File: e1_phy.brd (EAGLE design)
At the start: 100 x 75 mm, 136 parts, among them IC2 LD117AS33TR, IC3 LD117AS33TR, IC4 MCP4725, U1 XRT82D20, U2 GPS_GNS_2201, U3 VCTCXO-CONNORWINFIELD, U4 VCXO_TAITIEN_VT, X2 SMA-142-0701-801/806, X3 JACK2.5_SJ-2523, X4 0446200002

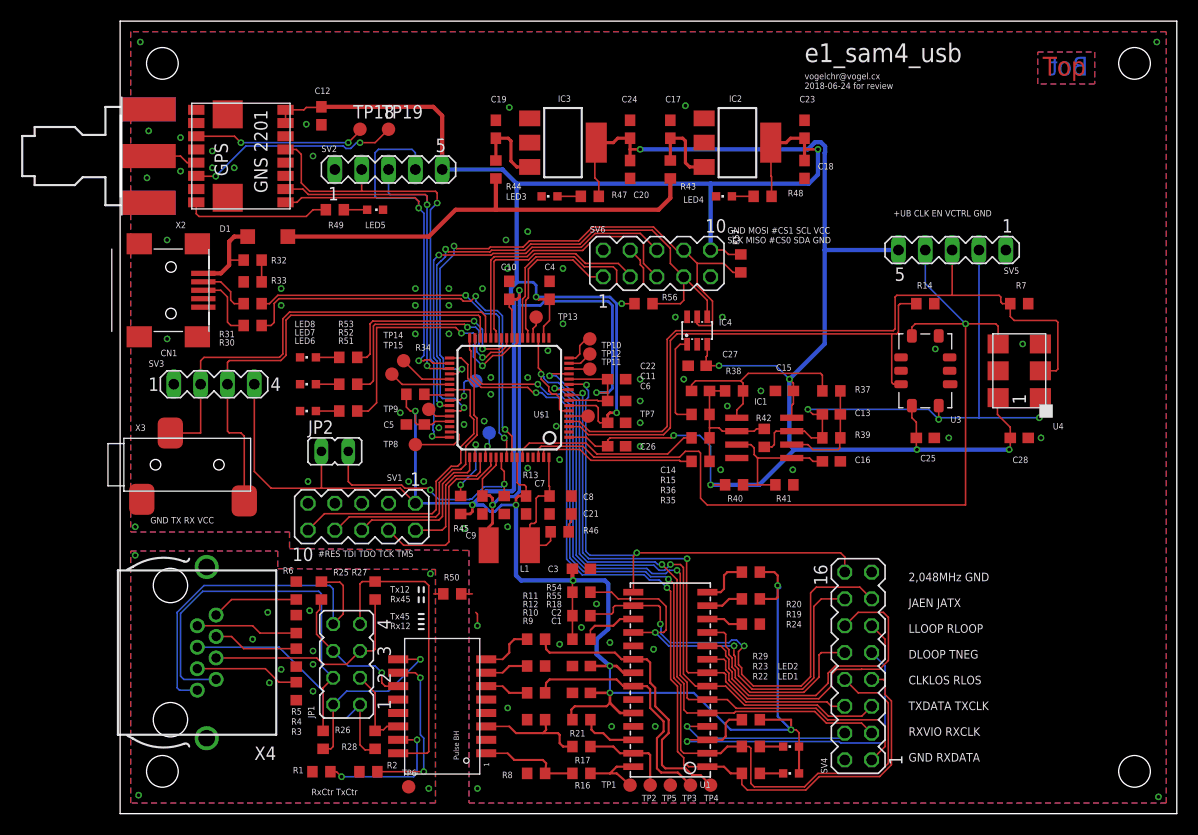
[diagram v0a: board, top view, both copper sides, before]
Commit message: Changed LIU to IDT82V2081.
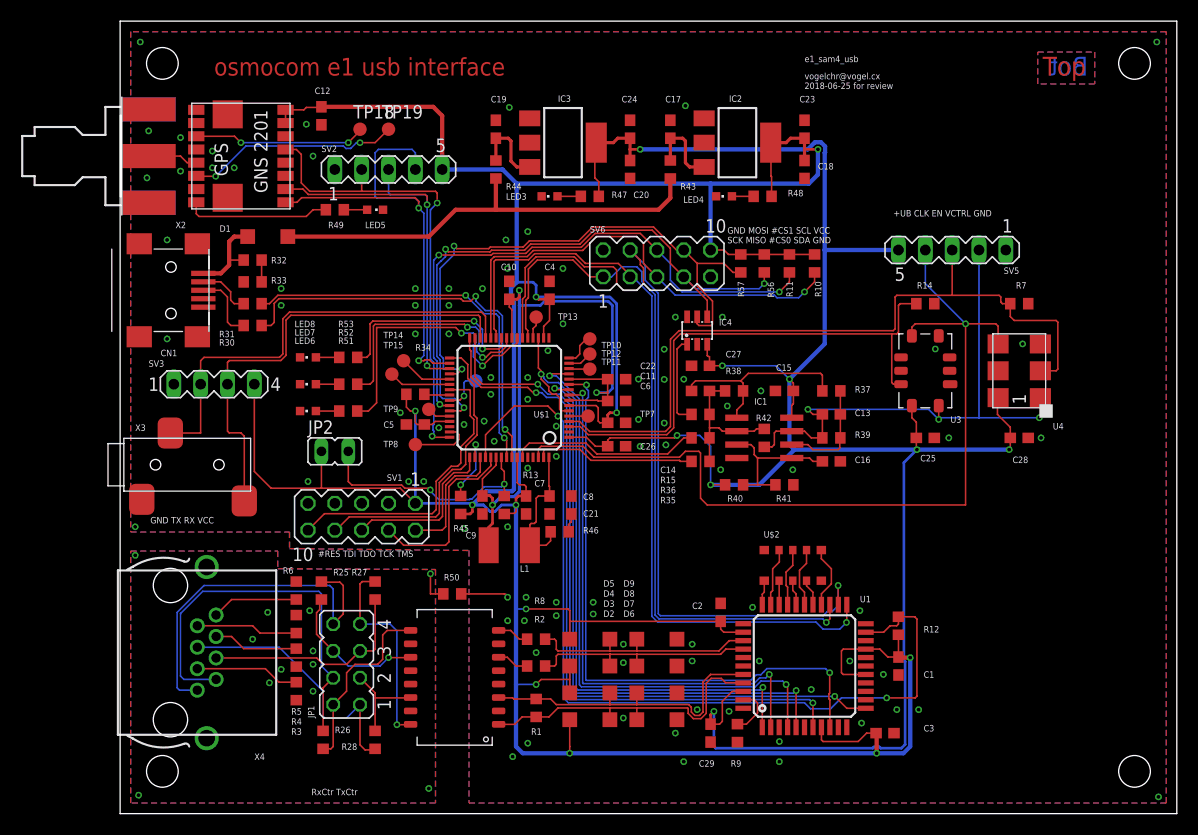
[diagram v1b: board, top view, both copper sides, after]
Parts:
- removed LED1, LED2: (no value), led:CHIPLED_0603
- removed R16, R17: 0R, rcl:R0603
- removed R18, R19, R20, R24: DNP, rcl:R0603
- removed R21, R22, R23, R29, R54, R55: 1k, rcl:R0603
- removed SV4: (no value), con-lstb:MA08-2
- removed TP1, TP17, TP2, TP3, TP4, TP5, TP6: TPB1,27, testpad:B1,27
- added C29: 100n, rcl:C0603
- added D2, D3, D4, D5, D6, D7, D8, D9: MBR0520LT, diode:SOD123
- added U$2: MNR 8x10k, laforge:MNR35
- C3: value 10u -> 100n
- R10, R11: value 9R1 -> 10k
- R12: value DNP -> 10k
- R8: value 60R -> DNP
- R9: value 60R -> 3k 1%
- TR1: value PE-65861 -> PULSE_T1094NL; device cvogel:PULSE_BH_XFORMER -> laforge:PULSE_BH
- U1: value XRT82D20 -> IDT82V2081; device cvogel:SOJ28/3 -> idt82v2081:TQFP44
- moved R10 48.4 mm to (65.7, 52.1), turned to 90 degrees
- moved R11 42.9 mm to (63.3, 52.1), turned to 90 degrees
- moved R12 34.5 mm to (73.7, 17.8), turned to 90 degrees
- moved C3 32.7 mm to (72.4, 7.62)
- moved C1 30.1 mm to (73.7, 14.0), turned to 270 degrees
- moved R1 21.2 mm to (39.4, 10.0), turned to 90 degrees
- moved R9 19.1 mm to (58.4, 7.62), turned to 270 degrees
- moved R2 18.8 mm to (39.4, 14.0), turned to 180 degrees
- moved C2 14.1 mm to (56.8, 19.1), turned to 90 degrees
- moved U1 12.8 mm to (64.8, 14.0)
- moved R8 12.7 mm to (39.4, 16.5)
- moved R56 12.0 mm to (61.0, 52.1), turned to 90 degrees
- moved TR1 2.77 mm to (31.6, 12.7), turned to 180 degrees
- moved C27 0.32 mm to (54.9, 42.4)
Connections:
- removed net #ATM: R24.1, U1.12
- removed net #CLKLOS: R23.1, SV4.8, U$1.31, U1.2
- removed net #DLOOP: SV4.10, U1.11
- removed net #LLOOP: SV4.12, U1.9
- removed net #RLOOP: SV4.11, U1.10
- removed net #RLOS: R22.1, SV4.7, U$1.32, U1.1
- removed net DIGI: R18.1, U1.17
- removed net JAEN: R54.2, SV4.14, U1.18
- removed net JATX: R55.2, SV4.13, U1.16
- removed net MUTERX: R21.1, U1.26
- removed net N$1: LED1.C, R22.2
- removed net N$2: LED2.C, R23.2
- removed net RAOS: R19.2, U1.13
- removed net RRING_LIU: R17.2, TP2.TP, U1.27
- removed net RTIP_LIU: R16.2, TP1.TP, U1.28
- removed net RX_PRI_CTR: R1.2, TR1.15
- removed net RX_VIOLATION: SV4.4, U1.4
- removed net TAOS: R20.2, U1.14
- removed net TNEG_CODE: R29.1, SV4.9, U1.3
- removed net TRING_XFMR: R11.1, TR1.8
- removed net TTIP_XFMR: R10.1, TR1.6
- removed net TX_PRI_CTR: R12.1, TR1.7
- removed net TX_SEC_CTR: R2.2, TR1.10
- new net #RST_LIU: U$1.31, U1.12
- new net #SPI_CS2: R11.1, SV6.6, U$1.42
- new net AD0: U$2.6, U1.26
- new net AD1: U$2.4, U1.27
- new net AD2: U$2.7, U1.28
- new net AD3: U$2.3, U1.29
- new net AD4: U$2.8, U1.30
- new net AD5: U$2.2, U1.31
- new net AD6: U$2.9, U1.32
- new net AD7: U$2.1, U1.33
- new net LOS_LIU: U$1.32, U1.7
- new net N$25: R8.2, TR1.8
- new net N$31: R9.1, U1.43
- net #SPI_CS0: now also R10.1
- net #SPI_CS1: now also R12.2, U$1.52, U1.21; no longer SV6.6, U$1.42
- net +UB: now also C29.1, U1.42
- net CLK2048: now also U1.9; no longer SV4.16, U1.15
- net GND: now also C29.2, D6.A, D7.A, D8.A, D9.A, U$2.10, U$2.5, U1.10, U1.11, U1.13, U1.14, U1.15, U1.17, U1.18, U1.22, U1.3, U1.38, U1.39, U1.44; no longer R12.2, R24.2, R8.2, SV4.15, SV4.2, TP5.TP, TR1.2, U1.19, U1.23, U1.25
- net GNDIO: no longer R1.1, R2.1, TP6.TP
- net N$5: now also R2.2, TR1.6; no longer TP17.TP, U$1.52
- net RRING: now also D3.A, D7.C, R1.2, U1.40; no longer R17.1, R9.1
- net RTIP: now also D2.A, D6.C, R1.1, U1.41; no longer R16.1, R8.1
- net RX_CLK: now also U1.4; no longer SV4.3, U1.5
- net RX_DATA: now also U1.5; no longer SV4.1, U1.6
- net SPI_MISO: now also U1.23
- net SPI_MOSI: now also U1.24
- net SPI_SCK: now also U1.25
- net TRING: now also D5.A, D9.C, R8.1, U1.36; no longer R11.2, TP4.TP, U1.20
- net TTIP: now also D4.A, D8.C, R2.1, U1.37; no longer R10.2, TP3.TP, U1.22
- net TX_CLK: now also U1.1; no longer SV4.5, U1.7
- net TX_DATA: now also U1.2; no longer SV4.6, U1.8
- net VCC: now also D2.C, D3.C, D4.C, D5.C, R10.2, R11.2, R12.1, U1.16, U1.19, U1.35, U1.8; no longer LED1.A, LED2.A, R18.2, R19.1, R20.1, R21.2, R29.2, R54.1, R55.1, U1.21, U1.24
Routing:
- net #CLKLOS: track 90.4 -> 0.00 mm, vias 2 -> 0
- net #RLOS: track 88.3 -> 0.00 mm, vias 2 -> 0
- net #RST_LIU: track 0.00 -> 69.8 mm, vias 0 -> 2
- net LOS_LIU: track 0.00 -> 67.3 mm, vias 0 -> 2
- net SPI_MOSI: track 24.4 -> 82.2 mm, vias 0 -> 1
- net +UB: track 140.7 -> 197.5 mm, vias 7 -> 8
- net SPI_SCK: track 14.8 -> 70.4 mm, vias 0 -> 1
- net #SPI_CS2: track 0.00 -> 54.1 mm, vias 0 -> 3
- net SPI_MISO: track 21.5 -> 75.5 mm, vias 0 -> 1
- net #SPI_CS1: track 37.7 -> 85.0 mm
- net JATX: track 43.2 -> 0.00 mm, vias 2 -> 0
- net JAEN: track 42.2 -> 0.00 mm, vias 2 -> 0
- net VCC: track 309.2 -> 347.7 mm, vias 12 -> 11
- net TNEG_CODE: track 34.5 -> 0.00 mm, vias 1 -> 0
- net #LLOOP: track 30.7 -> 0.00 mm
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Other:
- board text added: "osmocom e1 usb interface"
- board text added: "vogelchr@vogel.cx 2018-06-25 for review"
- board text removed: "2,048MHz GND JAEN JATX LLOOP RLOOP DLOOP TNEG CLKLOS RLOS TXDATA TXCLK RXVIO RXCLK GND RXDATA"
- board text removed: "Tx12 Rx45"
- board text removed: "Tx45 Rx12"
- board text removed: "vogelchr@vogel.cx 2018-06-24 for review"

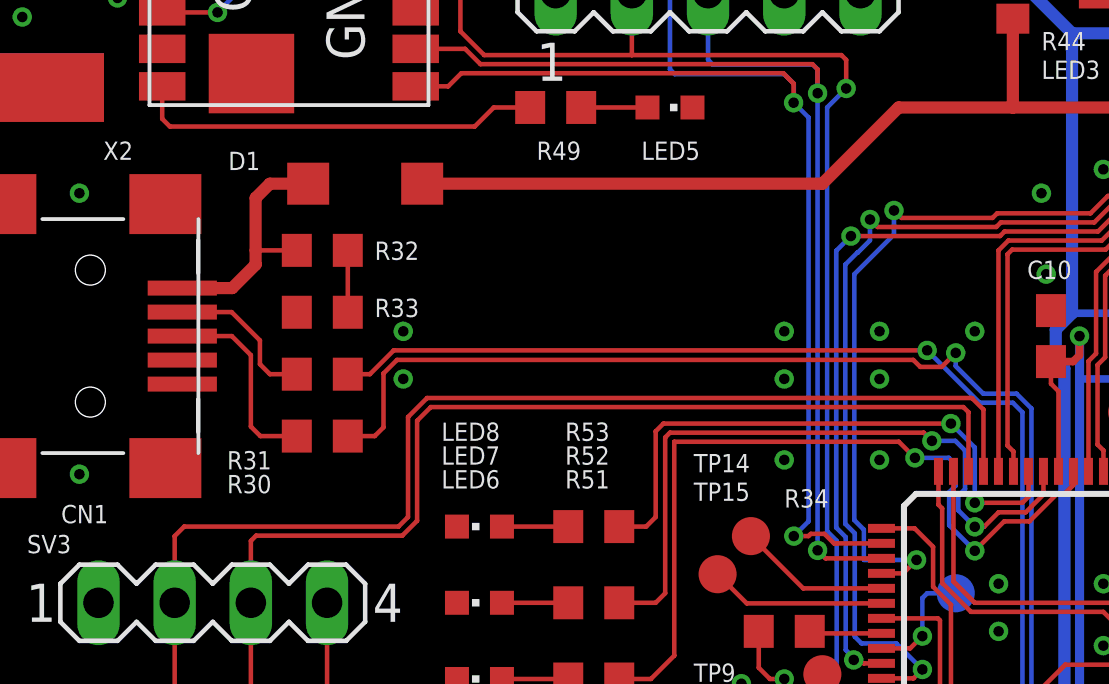
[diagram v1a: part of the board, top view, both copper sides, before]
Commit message: Implement review: ESD protection on USB.
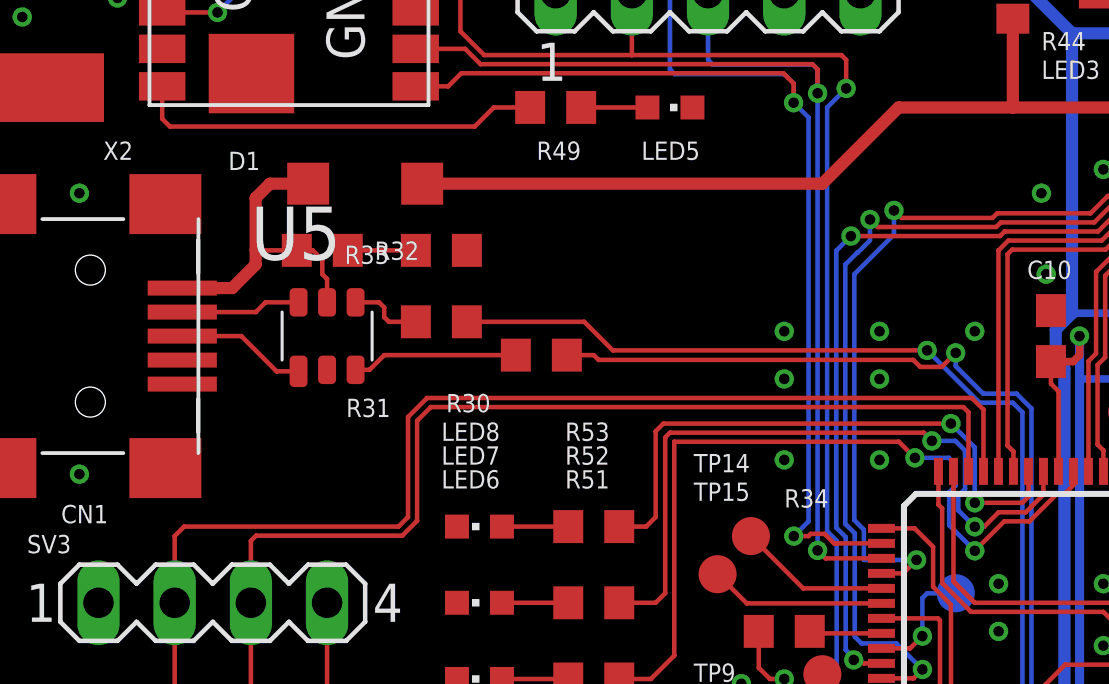
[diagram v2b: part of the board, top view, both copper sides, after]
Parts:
- added U5: IP4234CZ6, laforge:TSOP-6
- moved R30 7.79 mm to (19.8, 48.9)
- moved R33 4.47 mm to (16.5, 52.4), turned to 180 degrees
- moved R31 4.34 mm to (16.5, 50.0)
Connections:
- net USB_VBUS_CON renamed USB_VBUS
- removed net N$12: CN1.VBUS, D1.A, R32.2
- new net N$1: CN1.D+, U5.1
- new net N$2: CN1.D-, U5.6
- new net VBUS_CONN: CN1.VBUS, D1.A, R32.2, U5.5
- net GND: now also U5.2
- net USB_DDM_CON: now also U5.4; no longer CN1.D-
- net USB_DDP_CON: now also U5.3; no longer CN1.D+
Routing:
- net VBUS_CONN: track 0.00 -> 11.3 mm
- net USB_DDP: track 40.0 -> 30.7 mm
- net N$12: track 8.85 -> 0.00 mm
- net N$1: track 0.00 -> 4.36 mm
- net N$2: track 0.00 -> 4.01 mm
- net USB_DDM: track 37.2 -> 33.3 mm
- net USB_DDM_CON: track 5.14 -> 2.46 mm
- net USB_DDP_CON: track 6.59 -> 5.55 mm
- net GND: vias 98 -> 96
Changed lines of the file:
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@@
 <attribute name="VALUE" x="-2.54" y="52.84" size="1.27" layer="27" rot="R270"/>
 </element>
-<element name="R30" library="rcl" package="R0603" value="33R" x="12.54125" y="46.19625" smashed="yes" rot="R180">
-<attribute name="NAME" x="9.36625" y="44.29125" size="0.6096" layer="25" font="vector"/>
-<attribute name="VALUE" x="13.17625" y="48.10125" size="1.27" layer="27" rot="R180"/>
-</element>
-<element name="R31" library="rcl" package="R0603" value="33R" x="12.54125" y="48.26" smashed="yes" rot="R180">
-<attribute name="NAME" x="9.36625" y="45.085" size="0.6096" layer="25" font="vector"/>
-<attribute name="VALUE" x="13.17625" y="50.165" size="1.27" layer="27" rot="R180"/>
+<element name="R30" library="rcl" package="R0603" value="33R" x="19.84375" y="48.895" smashed="yes" rot="R180">
+<attribute name="NAME" x="16.66875" y="46.99" size="0.6096" layer="25" font="vector"/>
+<attribute name="VALUE" x="20.47875" y="50.8" size="1.27" layer="27" rot="R180"/>
+</element>
+<element name="R31" library="rcl" package="R0603" value="33R" x="16.51" y="50.00625" smashed="yes" rot="R180">
+<attribute name="NAME" x="13.335" y="46.83125" size="0.6096" layer="25" font="vector"/>
+<attribute name="VALUE" x="17.145" y="51.91125" size="1.27" layer="27" rot="R180"/>
 </element>
 <element name="R32" library="rcl" package="R0603" value="27k" x="12.54125" y="52.3875" smashed="yes" rot="R180">
@@
 <attribute name="VALUE" x="13.17625" y="54.2925" size="1.27" layer="27" rot="R180"/>
 </element>
-<element name="R33" library="rcl" package="R0603" value="47k" x="12.54125" y="50.32375" smashed="yes">
-<attribute name="NAME" x="14.2875" y="50.165" size="0.6096" layer="25" font="vector"/>
-<attribute name="VALUE" x="11.90625" y="48.41875" size="1.27" layer="27"/>
+<element name="R33" library="rcl" package="R0603" value="47k" x="16.51" y="52.3875" smashed="yes" rot="R180">
+<attribute name="NAME" x="14.76375" y="52.54625" size="0.6096" layer="25" font="vector" rot="R180"/>
+<attribute name="VALUE" x="17.145" y="54.2925" size="1.27" layer="27" rot="R180"/>
 </element>
 <element name="R34" library="rcl" package="R0603" value="DNP" x="27.94" y="39.6875" smashed="yes">
@@
 <attribute name="NAME" x="47.63625" y="21.47875" size="0.6096" layer="25" font="vector"/>
 <attribute name="VALUE" x="49.7" y="14.21" size="1.27" layer="27"/>
+</element>
+<element name="U5" library="laforge" package="TSOP-6" value="IP4234CZ6" x="12.7" y="49.53">
+<attribute name="OC_DIGIKEY" value="568-5869-1-ND" x="12.7" y="49.53" size="1.778" layer="27" display="off"/>
 </element>
 </elements>
@@
 <via x="27.94" y="49.68875" extent="1-16" drill="0.35"/>
 <via x="27.94" y="48.10125" extent="1-16" drill="0.35"/>
-<via x="15.24" y="48.10125" extent="1-16" drill="0.35"/>
-<via x="15.24" y="49.68875" extent="1-16" drill="0.35"/>
 <via x="31.115" y="45.4025" extent="1-16" drill="0.35"/>
 <via x="27.94" y="45.4025" extent="1-16" drill="0.35"/>
@@
 <wire x1="32.2825" y1="20.79625" x2="36.35375" y2="20.79625" width="0.1524" layer="1"/>
 <wire x1="36.35375" y1="20.79625" x2="36.67125" y2="20.47875" width="0.1524" layer="1" curve="-90"/>
+<contactref element="U5" pad="2"/>
 </signal>
 <signal name="LINE_PIN1">
@@
 <wire x1="68.77" y1="9.97" x2="67.6426" y2="11.0974" width="0.1524" layer="1"/>
 </signal>
-<signal name="USB_VBUS_CON">
+<signal name="USB_VBUS">
 <contactref element="R44" pad="2"/>
 <contactref element="R43" pad="2"/>
@@
 </signal>
 <signal name="USB_DDM_CON">
-<contactref element="CN1" pad="D-"/>
 <contactref element="R31" pad="2"/>
-<wire x1="7.874" y1="50.33" x2="9.51875" y2="50.33" width="0.1524" layer="1"/>
-<wire x1="11.69125" y1="48.26" x2="10.795" y2="48.26" width="0.1524" layer="1"/>
-<wire x1="10.4624" y1="48.5926" x2="10.795" y2="48.26" width="0.1524" layer="1"/>
-<wire x1="9.51875" y1="50.33" x2="10.4624" y2="49.38635" width="0.1524" layer="1"/>
-<wire x1="10.4624" y1="49.38635" x2="10.4624" y2="48.5926" width="0.1524" layer="1"/>
+<contactref element="U5" pad="4"/>
+<wire x1="13.65" y1="50.655" x2="14.4325" y2="50.655" width="0.1524" layer="1"/>
+<wire x1="14.4325" y1="50.655" x2="14.605" y2="50.4825" width="0.1524" layer="1"/>
+<wire x1="14.605" y1="50.4825" x2="14.605" y2="50.165" width="0.1524" layer="1"/>
+<wire x1="14.605" y1="50.165" x2="14.76375" y2="50.00625" width="0.1524" layer="1"/>
+<wire x1="14.76375" y1="50.00625" x2="15.66" y2="50.00625" width="0.1524" layer="1"/>
 </signal>
 <signal name="USB_DDP_CON">
-<contactref element="CN1" pad="D+"/>
 <contactref element="R30" pad="2"/>
-<wire x1="7.874" y1="49.53" x2="9.525" y2="49.53" width="0.1524" layer="1"/>
-<wire x1="9.525" y1="49.53" x2="10.16" y2="48.895" width="0.1524" layer="1"/>
-<wire x1="10.16" y1="46.51375" x2="10.4775" y2="46.19625" width="0.1524" layer="1"/>
-<wire x1="10.4775" y1="46.19625" x2="11.69125" y2="46.19625" width="0.1524" layer="1"/>
-<wire x1="10.16" y1="48.895" x2="10.16" y2="46.51375" width="0.1524" layer="1"/>
+<contactref element="U5" pad="3"/>
+<wire x1="13.65" y1="48.405" x2="14.115" y2="48.405" width="0.1524" layer="1"/>
+<wire x1="14.115" y1="48.405" x2="14.605" y2="48.895" width="0.1524" layer="1"/>
+<wire x1="14.605" y1="48.895" x2="18.99375" y2="48.895" width="0.1524" layer="1"/>
 </signal>
 <signal name="USB_VBUS_SENS">
 <contactref element="R32" pad="1"/>
 <contactref element="R33" pad="2"/>
-<wire x1="13.39125" y1="50.32375" x2="13.39125" y2="52.3875" width="0.1524" layer="1"/>
+<wire x1="15.66" y1="52.3875" x2="13.39125" y2="52.3875" width="0.1524" layer="1"/>
 </signal>
 <signal name="USB_DDP">
@@
 <wire x1="35.6852625" y1="47.6099" x2="36.1799" y2="47.1152625" width="0.1524" layer="16"/>
 <wire x1="34.5740125" y1="47.6099" x2="35.6852625" y2="47.6099" width="0.1524" layer="16"/>
-<wire x1="15.0326625" y1="48.73625" x2="14.58070625" y2="48.28429375" width="0.1524" layer="1"/>
-<wire x1="14.58070625" y1="48.28429375" x2="14.58070625" y2="46.48945625" width="0.1524" layer="1"/>
-<wire x1="14.58070625" y1="46.48945625" x2="14.2875" y2="46.19625" width="0.1524" layer="1"/>
-<wire x1="14.2875" y1="46.19625" x2="13.39125" y2="46.19625" width="0.1524" layer="1"/>
-<wire x1="32.24048125" y1="48.73625" x2="15.0326625" y2="48.73625" width="0.1524" layer="1"/>
+<wire x1="21.74875" y1="48.73625" x2="21.59" y2="48.895" width="0.1524" layer="1"/>
+<wire x1="21.59" y1="48.895" x2="20.69375" y2="48.895" width="0.1524" layer="1"/>
+<wire x1="32.24048125" y1="48.73625" x2="21.74875" y2="48.73625" width="0.1524" layer="1"/>
 </signal>
 <signal name="USB_DDM">
@@
 <wire x1="35.56" y1="47.3075" x2="34.44875" y2="47.3075" width="0.1524" layer="16"/>
 <wire x1="34.44875" y1="47.3075" x2="32.7025" y2="49.05375" width="0.1524" layer="16"/>
-<wire x1="13.39125" y1="48.26" x2="14.12875" y2="48.26" width="0.1524" layer="1"/>
-<wire x1="14.12875" y1="48.26" x2="14.9225" y2="49.05375" width="0.1524" layer="1"/>
-<wire x1="14.9225" y1="49.05375" x2="32.7025" y2="49.05375" width="0.1524" layer="1"/>
+<wire x1="17.36" y1="50.00625" x2="21.2725" y2="50.00625" width="0.1524" layer="1"/>
+<wire x1="21.2725" y1="50.00625" x2="22.225" y2="49.05375" width="0.1524" layer="1"/>
+<wire x1="22.225" y1="49.05375" x2="32.7025" y2="49.05375" width="0.1524" layer="1"/>
 </signal>
 <signal name="TST">
@@
 <wire x1="23.38" y1="57.15" x2="21.17" y2="57.15" width="0.1524" layer="1"/>
 </signal>
-<signal name="N$12">
+<signal name="VBUS_CONN">
 <contactref element="CN1" pad="VBUS"/>
 <contactref element="R32" pad="2"/>
@@
 <wire x1="11.69125" y1="52.3875" x2="12.07" y2="52.76625" width="0.15" layer="1"/>
 <wire x1="11.69125" y1="52.3875" x2="10.31875" y2="52.3875" width="0.1524" layer="1"/>
+<contactref element="U5" pad="5"/>
+<wire x1="12.7" y1="50.655" x2="12.7" y2="51.435" width="0.1524" layer="1"/>
+<wire x1="12.7" y1="51.435" x2="12.54125" y2="51.59375" width="0.1524" layer="1"/>
+<wire x1="12.54125" y1="52.07" x2="12.54125" y2="51.59375" width="0.1524" layer="1"/>
+<wire x1="11.69125" y1="52.3875" x2="12.22375" y2="52.3875" width="0.1524" layer="1"/>
+<wire x1="12.22375" y1="52.3875" x2="12.54125" y2="52.07" width="0.1524" layer="1"/>
 </signal>
 <signal name="SAM4S_CLK">
@@
 <wire x1="59.27" y1="8.47" x2="60.325" y2="9.525" width="0.1524" layer="1"/>
 </signal>
+<signal name="N$1">
+<contactref element="CN1" pad="D+"/>
+<contactref element="U5" pad="1"/>
+<wire x1="9.8425" y1="49.53" x2="7.874" y2="49.53" width="0.1524" layer="1"/>
+<wire x1="11.75" y1="48.355" x2="11.0175" y2="48.355" width="0.1524" layer="1"/>
+<wire x1="11.0175" y1="48.355" x2="9.8425" y2="49.53" width="0.1524" layer="1"/>
+</signal>
+<signal name="N$2">
+<contactref element="CN1" pad="D-"/>
+<contactref element="U5" pad="6"/>
+<wire x1="7.874" y1="50.33" x2="10.325" y2="50.33" width="0.1524" layer="1"/>
+<wire x1="10.65" y1="50.655" x2="11.75" y2="50.655" width="0.1524" layer="1"/>
+<wire x1="10.325" y1="50.33" x2="10.65" y2="50.655" width="0.1524" layer="1"/>
+</signal>
 </signals>
